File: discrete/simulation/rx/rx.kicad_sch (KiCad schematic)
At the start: 22 parts, among them Q1 2N5551, Q2 2N5401, Q200 2N5401, Q3 2N5401

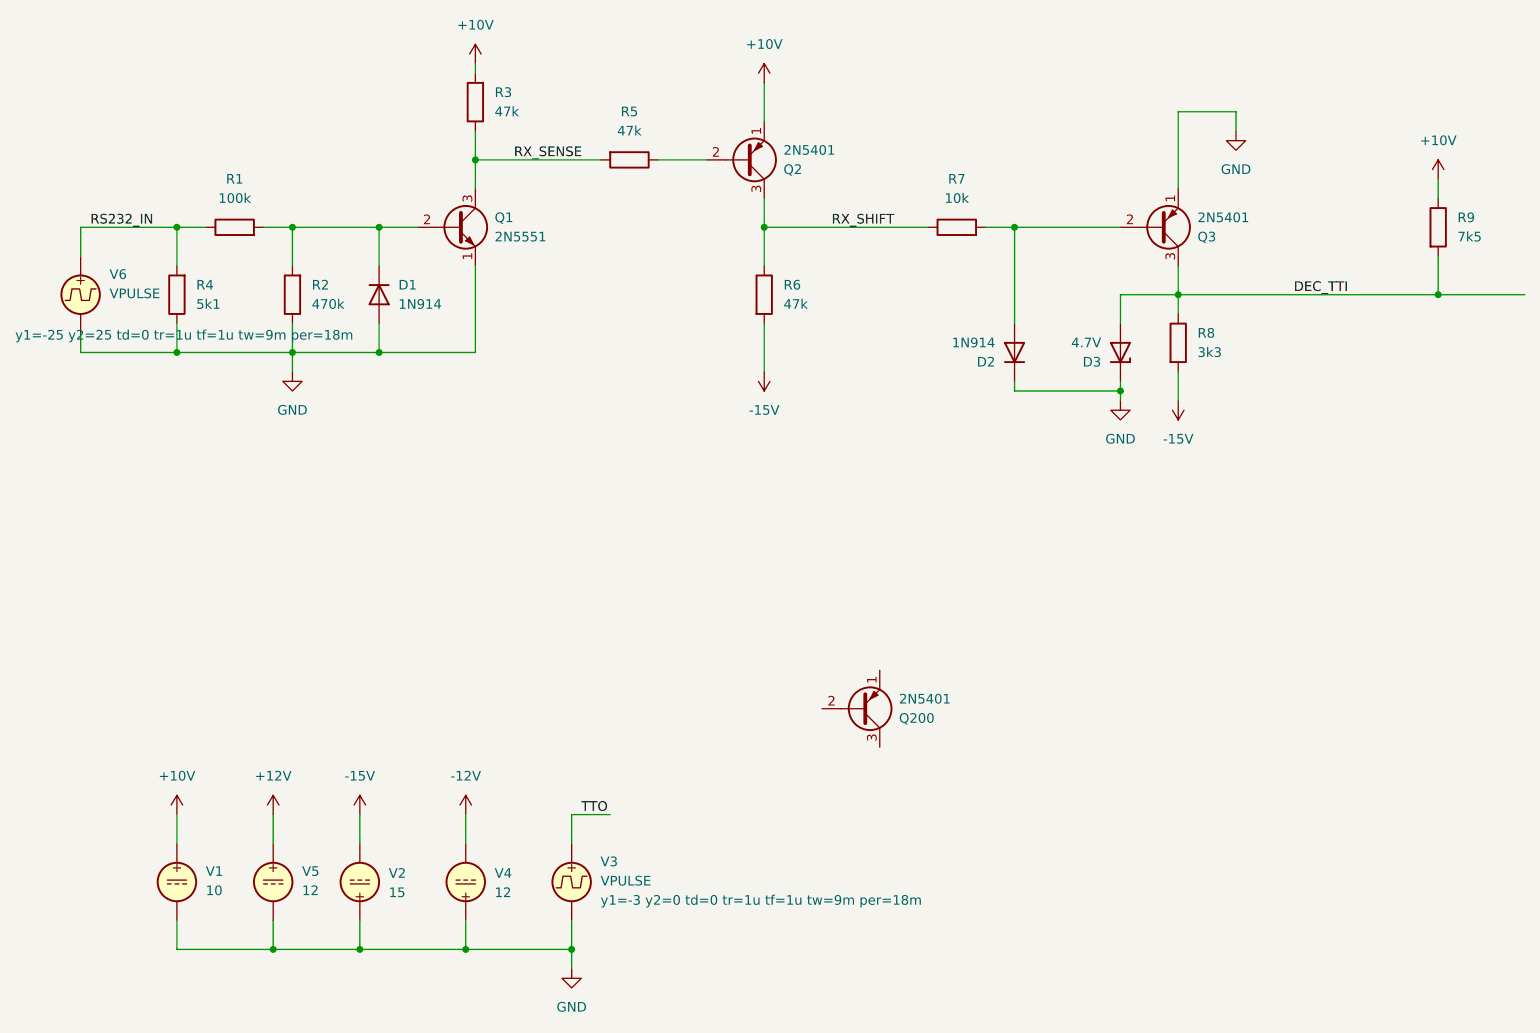
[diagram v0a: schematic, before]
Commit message: Validate discrete RS232 receiver across voltage, load and speed conditions
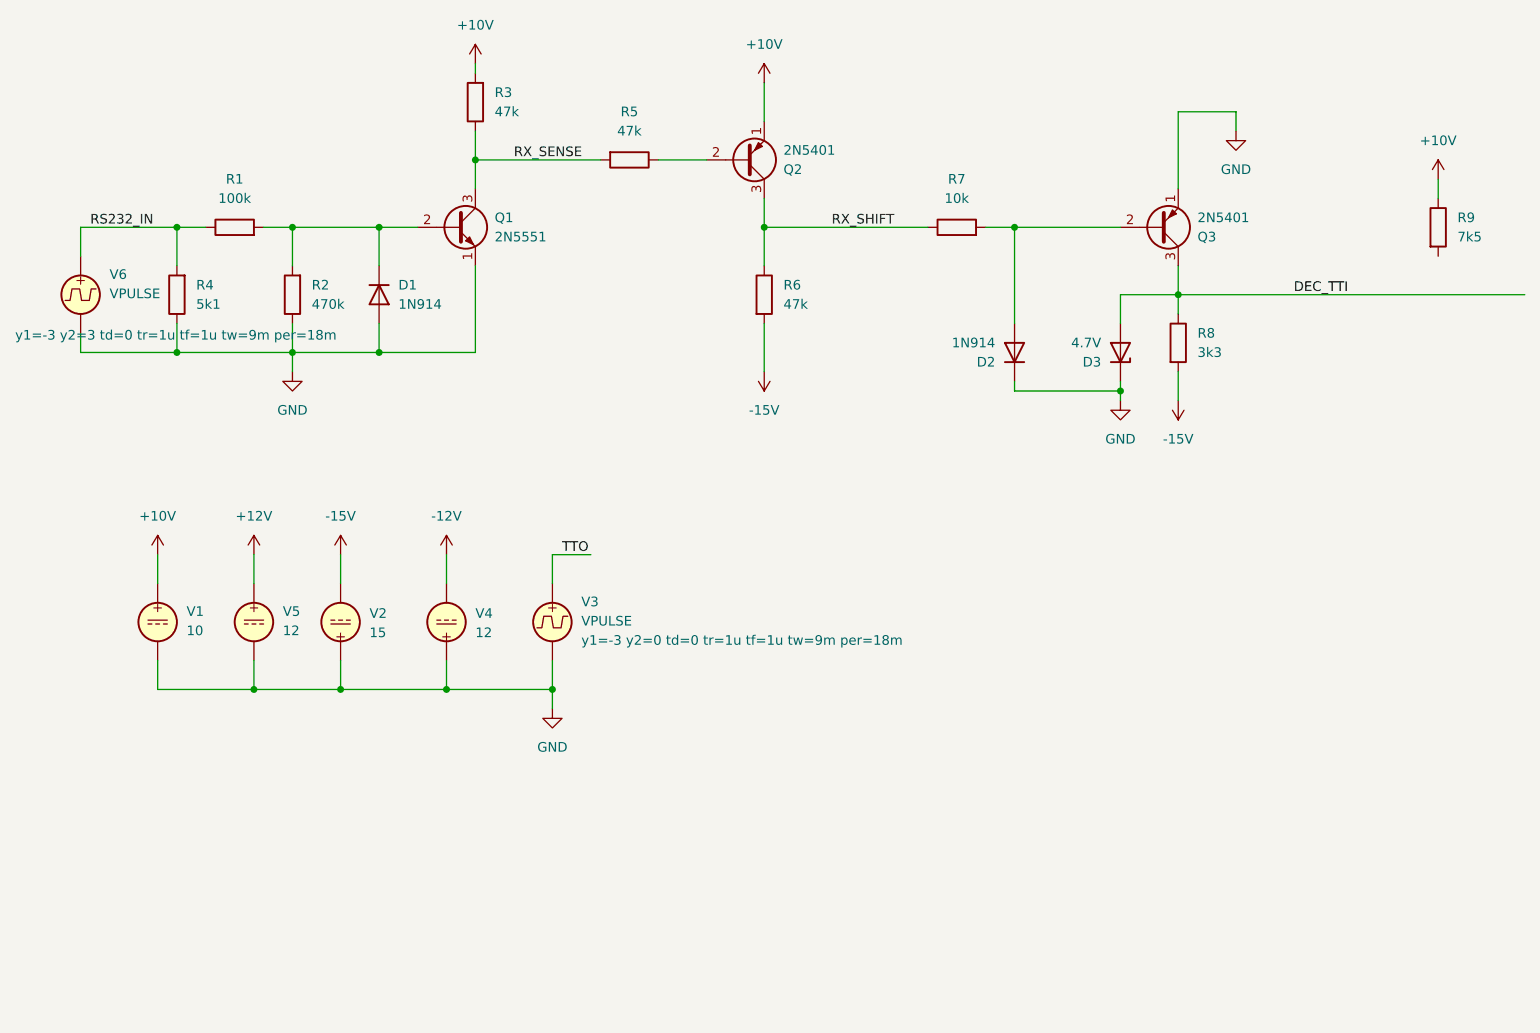
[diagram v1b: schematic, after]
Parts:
- removed Q200: 2N5401, Package_TO_SOT_THT:TO-92_Inline, symbol Transistor_BJT:2N3906
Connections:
- net DEC_TTI: no longer R9.2
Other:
- moved on the sheet: V1, V2, V3, V4, V5

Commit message: Final Rx modeling
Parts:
- added R10: 2k7, symbol Device:R
- R8: value 3k3 -> 2k2
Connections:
- net DEC_TTI: now also R10.1; no longer D3.2 (A)
- net GND: now also R10.2; no longer D3.1 (K)
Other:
- note added: "1/2W"
- moved on the sheet: D3
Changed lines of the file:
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@@
 	(generator_version "9.0")
 	(paper "A4")
+	(text "1/2W"
+		(exclude_from_sim no)
+		(at 37.846 71.12 0)
+		(effects
+			(font
+				(size 1.27 1.27)
+			)
+		)
+	)
+	(text "1/2W"
+		(exclude_from_sim no)
+		(at 169.672 77.47 0)
+		(effects
+			(font
+				(size 1.27 1.27)
+			)
+		)
+	)
 	(junction
 		(at 73.66 123.19)
@@
 	(wire
 		(pts
-			(xy 162.56 74.93) (xy 162.56 71.12)
+			(xy 170.18 71.12) (xy 215.9 71.12)
+		)
+		(stroke
+			(width 0)
+			(type default)
+		)
+	)
+	(wire
+		(pts
+			(xy 162.56 73.66) (xy 162.56 71.12)
 		)
 		(stroke
@@
 	(wire
 		(pts
-			(xy 162.56 82.55) (xy 162.56 83.82)
-		)
-		(stroke
-			(width 0)
-			(type default)
-		)
-	)
-	(wire
-		(pts
-			(xy 170.18 71.12) (xy 215.9 71.12)
+			(xy 162.56 81.28) (xy 162.56 83.82)
 		)
 		(stroke
@@
 			)
 		)
-		(property "Value" "3k3"
+		(property "Value" "2k2"
 			(at 172.72 78.7399 0)
 			(effects
@@
 	(symbol
 		(lib_id "Device:D_Zener")
-		(at 162.56 78.74 270)
+		(at 172.72 113.03 270)
 		(mirror x)
 		(unit 1)
@@
 		(dnp no)
 		(property "Reference" "D3"
-			(at 160.02 80.0101 90)
+			(at 170.18 114.3001 90)
 			(effects
 				(font
@@
 		)
 		(property "Value" "4.7V"
-			(at 160.02 77.4701 90)
+			(at 170.18 111.7601 90)
 			(effects
 				(font
@@
 		)
 		(property "Footprint" ""
-			(at 162.56 78.74 0)
+			(at 172.72 113.03 0)
 			(effects
 				(font
@@
 		)
 		(property "Datasheet" "~"
-			(at 162.56 78.74 0)
+			(at 172.72 113.03 0)
 			(effects
 				(font
@@
 		)
 		(property "Description" "Zener diode"
-			(at 162.56 78.74 0)
+			(at 172.72 113.03 0)
 			(effects
 				(font
@@
 		)
 		(property "Sim.Library" "/home/sfinneran/work/ACMS/PDP-8-Serial/discrete/simulation/models/zener_4v7.lib"
-			(at 162.56 78.74 0)
+			(at 172.72 113.03 0)
 			(effects
 				(font
@@
 		)
 		(property "Sim.Name" "D4V7"
-			(at 162.56 78.74 0)
+			(at 172.72 113.03 0)
 			(effects
 				(font
@@
 		)
 		(property "Sim.Device" "D"
-			(at 162.56 78.74 0)
+			(at 172.72 113.03 0)
 			(effects
 				(font
@@
 		)
 		(property "Sim.Pins" "1=K 2=A"
-			(at 162.56 78.74 0)
+			(at 172.72 113.03 0)
 			(effects
 				(font
@@
 					(unit 1)
 				)
+			)
+		)
+	)
+	(symbol
+		(lib_id "Device:R")
+		(at 162.56 77.47 0)
+		(mirror y)
+		(unit 1)
+		(exclude_from_sim no)
+		(in_bom yes)
+		(on_board yes)
+		(dnp no)
+		(property "Reference" "R10"
+			(at 160.02 76.1999 0)
+			(effects
+				(font
+					(size 1.27 1.27)
+				)
+				(justify left)
+			)
+		)
+		(property "Value" "2k7"
+			(at 160.02 78.7399 0)
+			(effects
+				(font
+					(size 1.27 1.27)
+				)
+				(justify left)
+			)
+		)
+		(property "Footprint" ""
+			(at 164.338 77.47 90)
+			(effects
+				(font
+					(size 1.27 1.27)
+				)
+				(hide yes)
+			)
+		)
+		(property "Datasheet" "~"
+			(at 162.56 77.47 0)
+			(effects
+				(font
+					(size 1.27 1.27)
+				)
+				(hide yes)
+			)
+		)
+		(property "Description" "Resistor"
+			(at 162.56 77.47 0)
+			(effects
+				(font
+					(size 1.27 1.27)
+				)
+				(hide yes)
+			)
+		)
+		(pin "1"
+		)
+		(pin "2"
+		)
+		(instances
+			(project "rx"
+				(path "/f7e369c0-c7d8-4213-ba85-708f7769f576"
+					(reference "R10")
+					(unit 1)
+				)
